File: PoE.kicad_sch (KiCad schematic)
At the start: 24 parts, among them IC1 TPS2378DDA

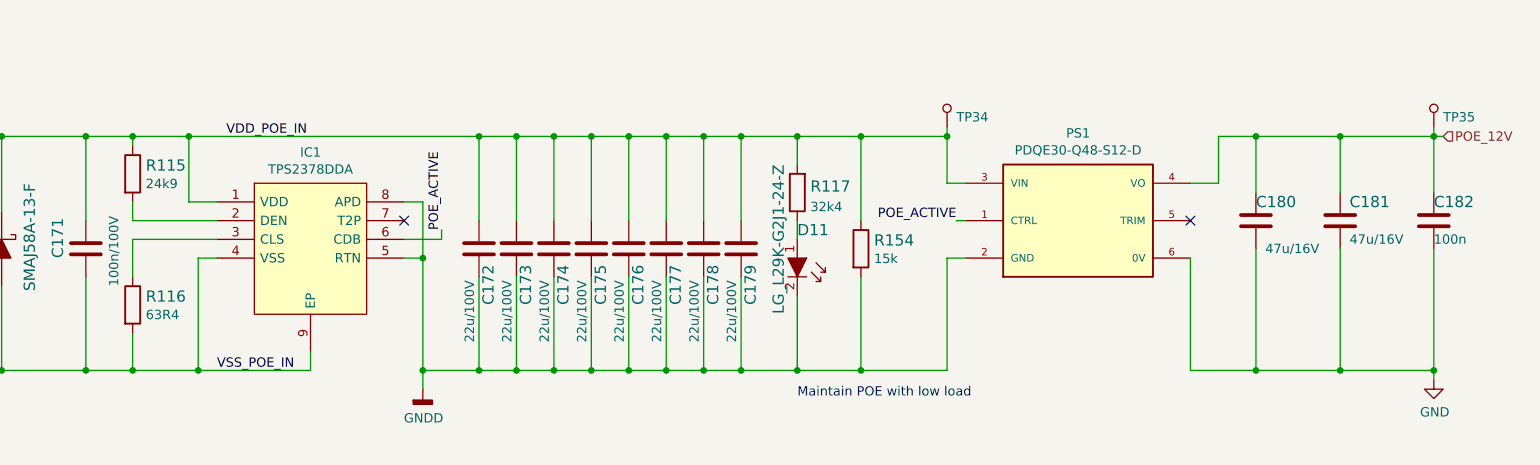
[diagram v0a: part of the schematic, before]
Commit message: Added cosmetic changes to schematics (e.g. position of labels, designators)
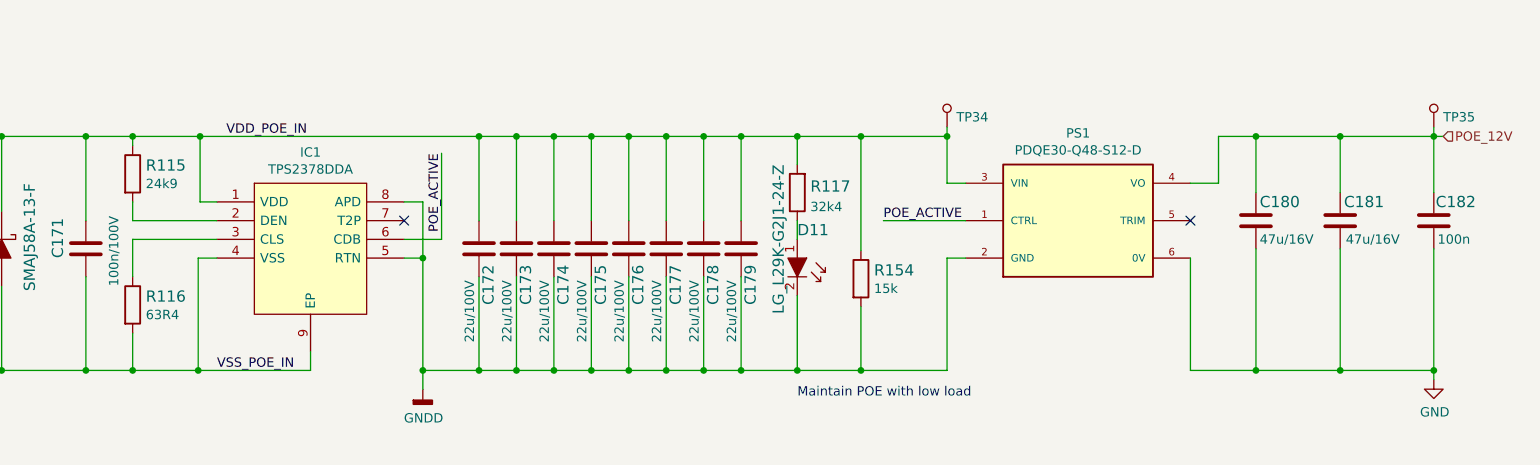
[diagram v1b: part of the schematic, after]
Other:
- moved on the sheet: R154
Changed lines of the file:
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@@
   (junction (at 90.17 87.63) (diameter 0) (color 0 0 0 0)
   )
-  (junction (at 104.14 87.63) (diameter 0) (color 0 0 0 0)
+  (junction (at 105.664 87.63) (diameter 0) (color 0 0 0 0)
   )
   (junction (at 153.67 119.38) (diameter 0) (color 0 0 0 0)
@@
     (stroke (width 0) (type default) (color 0 0 0 0))
   )
-  (wire (pts (xy 104.14 87.63) (xy 104.14 96.52))
+  (wire (pts (xy 105.664 87.63) (xy 105.664 96.52))
     (stroke (width 0) (type default) (color 0 0 0 0))
   )
@@
     (stroke (width 0) (type default) (color 0 0 0 0))
   )
+  (wire (pts (xy 105.664 87.63) (xy 143.51 87.63))
+    (stroke (width 0) (type default) (color 0 0 0 0))
+  )
   (wire (pts (xy 143.51 99.06) (xy 143.51 87.63))
     (stroke (width 0) (type default) (color 0 0 0 0))
@@
     (stroke (width 0) (type default) (color 0 0 0 0))
   )
-  (wire (pts (xy 104.14 96.52) (xy 107.95 96.52))
+  (wire (pts (xy 105.664 96.52) (xy 107.95 96.52))
     (stroke (width 0) (type default) (color 0 0 0 0))
   )
@@
     (stroke (width 0) (type default) (color 0 0 0 0))
   )
-  (wire (pts (xy 104.14 87.63) (xy 143.51 87.63))
+  (wire (pts (xy 96.52 87.63) (xy 105.664 87.63))
     (stroke (width 0) (type default) (color 0 0 0 0))
   )
@@
     (stroke (width 0) (type default) (color 0 0 0 0))
   )
-  (wire (pts (xy 195.326 106.68) (xy 195.326 119.38))
+  (wire (pts (xy 195.326 110.744) (xy 195.326 119.38))
     (stroke (width 0) (type default) (color 0 0 0 0))
   )
@@
     (stroke (width 0) (type default) (color 0 0 0 0))
   )
-  (wire (pts (xy 195.326 99.06) (xy 195.326 87.63))
+  (wire (pts (xy 195.326 103.124) (xy 195.326 87.63))
     (stroke (width 0) (type default) (color 0 0 0 0))
   )
@@
     (stroke (width 0) (type default) (color 0 0 0 0))
   )
-  (wire (pts (xy 96.52 87.63) (xy 104.14 87.63))
-    (stroke (width 0) (type default) (color 0 0 0 0))
-  )
   (wire (pts (xy 66.04 113.03) (xy 68.58 113.03))
     (stroke (width 0) (type default) (color 0 0 0 0))
@@
     (stroke (width 0) (type default) (color 0 0 0 0))
   )
-  (wire (pts (xy 208.28 99.06) (xy 209.55 99.06))
+  (wire (pts (xy 198.374 99.06) (xy 209.55 99.06))
     (stroke (width 0) (type default) (color 0 0 0 0))
   )
@@
     (stroke (width 0) (type default) (color 0 0 0 0))
   )
-  (wire (pts (xy 138.43 101.6) (xy 138.43 100.33))
+  (wire (pts (xy 138.43 101.6) (xy 138.43 89.916))
     (stroke (width 0) (type default) (color 0 0 0 0))
   )
@@
     (effects (font (size 1.27 1.27)) (justify left bottom))
   )
-  (label "POE_ACTIVE" (at 208.28 99.06 180)
-    (effects (font (size 1.27 1.27)) (justify right bottom))
+  (label "POE_ACTIVE" (at 198.374 99.06 0)
+    (effects (font (size 1.27 1.27)) (justify left bottom))
   )
   (label "POE_VC4" (at 33.02 118.11 0)
@@
     (effects (font (size 1.27 1.27)) (justify left bottom))
   )
-  (label "POE_ACTIVE" (at 138.43 100.33 90)
-    (effects (font (size 1.27 1.27)) (justify left bottom))
+  (label "POE_ACTIVE" (at 138.43 89.916 270)
+    (effects (font (size 1.27 1.27)) (justify right bottom))
   )
   (label "VSS_POE_IN" (at 107.95 119.38 0)
@@
   (symbol (lib_id "kria-k26-devboard:C_47u_16V_1206") (at 248.92 99.06 0) (unit 1)
     (in_bom yes) (on_board yes)
-    (property "Reference" "C180" (id 0) (at 248.92 96.52 0)
+    (property "Reference" "C180" (id 0) (at 249.428 96.52 0)
       (effects (font (size 1.524 1.524)) (justify left))
     )
@@
       (effects (font (size 1.524 1.524)) (justify left) hide)
     )
-    (property "Val" "47u/16V" (id 6) (at 250.19 102.87 0)
+    (property "Val" "47u/16V" (id 6) (at 249.428 101.6 0)
       (effects (font (size 1.27 1.27)) (justify left))
     )
@@
   (symbol (lib_id "kria-k26-devboard:C_47u_16V_1206") (at 260.35 99.06 0) (unit 1)
     (in_bom yes) (on_board yes)
-    (property "Reference" "C181" (id 0) (at 261.62 96.52 0)
+    (property "Reference" "C181" (id 0) (at 260.858 96.52 0)
       (effects (font (size 1.524 1.524)) (justify left))
     )
@@
       (effects (font (size 1.524 1.524)) (justify left) hide)
     )
-    (property "Val" "47u/16V" (id 6) (at 261.62 101.6 0)
+    (property "Val" "47u/16V" (id 6) (at 261.112 101.6 0)
       (effects (font (size 1.27 1.27)) (justify left))
     )
@@
   (symbol (lib_id "kria-k26-devboard:C_100n_0402_16V") (at 273.05 99.06 0) (unit 1)
     (in_bom yes) (on_board yes)
-    (property "Reference" "C182" (id 0) (at 273.05 96.52 0)
+    (property "Reference" "C182" (id 0) (at 273.304 96.52 0)
       (effects (font (size 1.524 1.524)) (justify left))
     )
@@
       (effects (font (size 1.524 1.524)) (justify left) hide)
     )
-    (property "Val" "100n" (id 6) (at 273.05 101.6 0)
+    (property "Val" "100n" (id 6) (at 273.558 101.6 0)
       (effects (font (size 1.27 1.27)) (justify left))
     )
@@
     (pin "2")
   )
-  (symbol (lib_id "kria-k26-devboard:R_15k_2010") (at 195.326 102.87 270) (unit 1)
+  (symbol (lib_id "kria-k26-devboard:R_15k_2010") (at 195.326 106.934 270) (unit 1)
     (in_bom yes) (on_board yes)
-    (property "Reference" "R154" (id 0) (at 197.104 101.727 90)
+    (property "Reference" "R154" (id 0) (at 197.104 105.791 90)
       (effects (font (size 1.524 1.524)) (justify left))
     )
-    (property "Value" "R_15k_2010" (id 1) (at 191.516 102.87 0)
+    (property "Value" "R_15k_2010" (id 1) (at 191.516 106.934 0)
       (effects (font (size 1.524 1.524)) hide)
     )
-    (property "Footprint" "kria-k26-devboard-footprints:2010-res" (id 2) (at 200.406 107.95 0)
-      (effects (font (size 1.524 1.524)) (justify left) hide)
-    )
-    (property "Datasheet" "" (id 3) (at 195.326 102.87 0)
+    (property "Footprint" "kria-k26-devboard-footprints:2010-res" (id 2) (at 200.406 112.014 0)
+      (effects (font (size 1.524 1.524)) (justify left) hide)
+    )
+    (property "Datasheet" "" (id 3) (at 195.326 106.934 0)
       (effects (font (size 1.27 1.27)) hide)
     )
-    (property "Manufacturer" "TE Connectivity Passive Product" (id 4) (at 205.486 107.95 0)
-      (effects (font (size 1.524 1.524)) (justify left) hide)
-    )
-    (property "MPN" "CRGCQ2010F15K" (id 5) (at 202.946 107.95 0)
-      (effects (font (size 1.524 1.524)) (justify left) hide)
-    )
-    (property "Val" "15k" (id 6) (at 197.104 104.2162 90)
+    (property "Manufacturer" "TE Connectivity Passive Product" (id 4) (at 205.486 112.014 0)
+      (effects (font (size 1.524 1.524)) (justify left) hide)
+    )
+    (property "MPN" "CRGCQ2010F15K" (id 5) (at 202.946 112.014 0)
+      (effects (font (size 1.524 1.524)) (justify left) hide)
+    )
+    (property "Val" "15k" (id 6) (at 197.104 108.2802 90)
       (effects (font (size 1.27 1.27)) (justify left))
     )

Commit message: Bump date and revision
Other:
- title: PoE -> Kria K26 Devboard
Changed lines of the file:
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@@
   (paper "A4")
   (title_block
-    (title "PoE")
-    (date "2022-07-25")
-    (rev "1.1.0")
+    (title "Kria K26 Devboard")
+    (date "2023-02-15")
+    (rev "1.1.1")
     (comment 1 "www.antmicro.com")
     (comment 2 "Antmicro Ltd.")

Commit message: Bom optimization
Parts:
- C176, C177, C178, C179: DNP (none) -> DNP
